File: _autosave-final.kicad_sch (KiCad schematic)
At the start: 25 parts, among them J1 Conn_02x16_Odd_Even, J3 USB_C_Receptacle_USB2.0_14P, SW1 SW_Push, U2 INA219AxD, U3 BQ25601, U4 CH224K

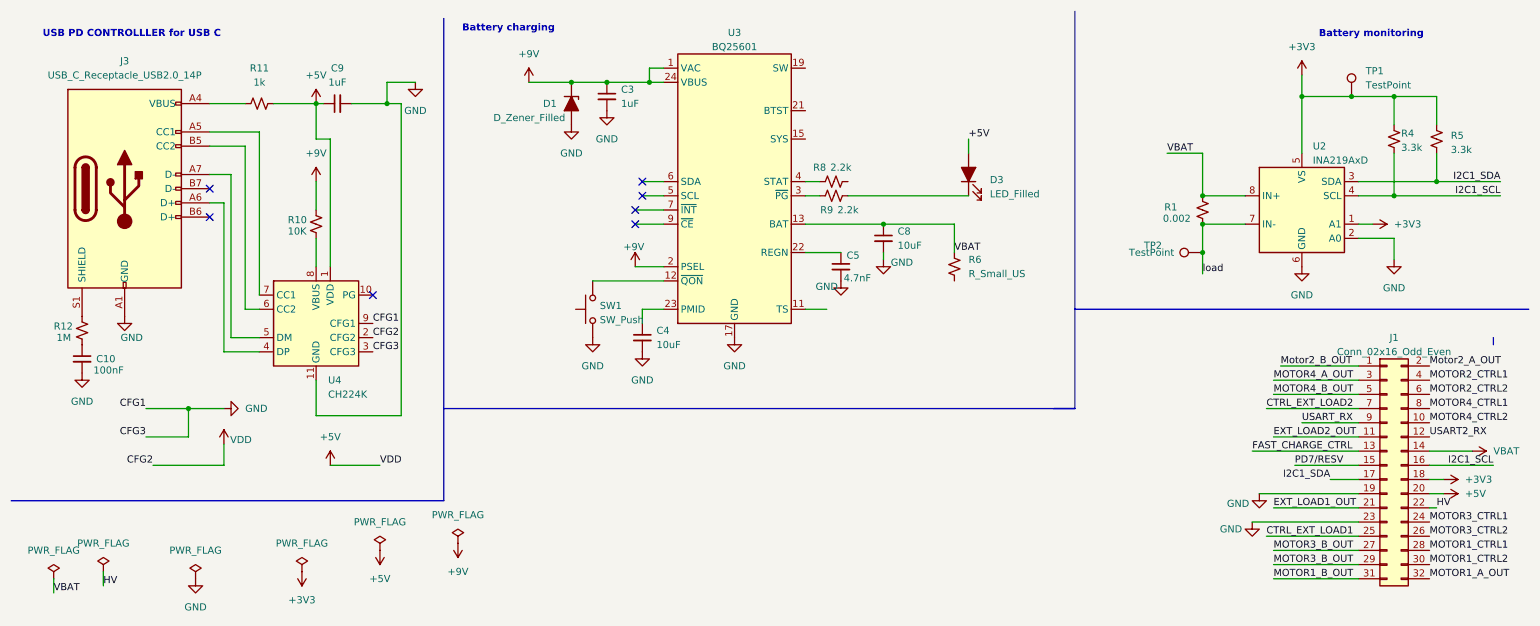
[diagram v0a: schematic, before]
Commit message: i changed my battery monitoring ic
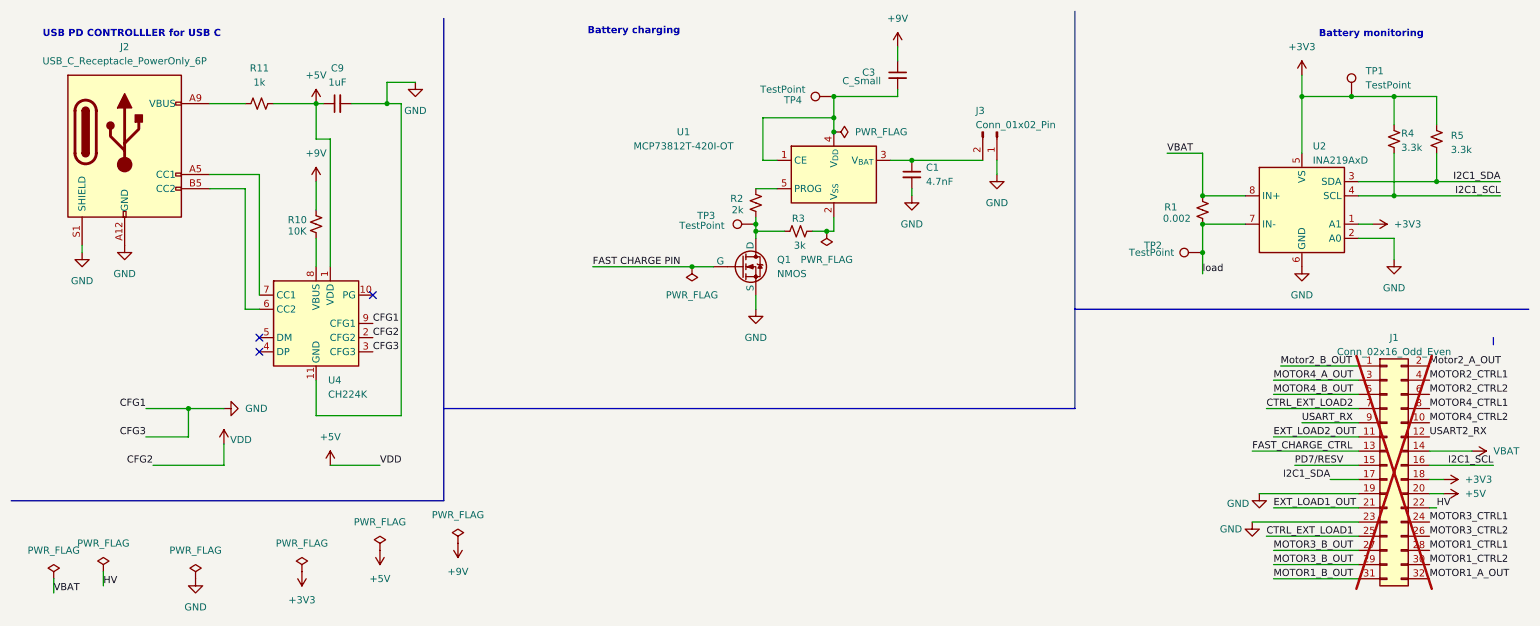
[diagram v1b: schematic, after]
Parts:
- removed C10: 100nF, symbol Device:C_Small
- removed C4: 10uF, Capacitor_SMD:CP_Elec_3x5.3, symbol Device:C_Small
- removed C5: 4.7nF, symbol Device:C_Small
- removed C8: 10uF, symbol Device:C_Small
- removed D1: D_Zener_Filled, symbol Device:D_Zener_Filled
- removed D3: LED_Filled, symbol Device:LED_Filled
- removed J3: USB_C_Receptacle_USB2.0_14P, symbol Connector:USB_C_Receptacle_USB2.0_14P
- removed R12: 1M, symbol Device:R_Small_US
- removed R6: R_Small_US, symbol Device:R_Small_US
- removed R8, R9: 2.2k, symbol Device:R_Small_US
- removed SW1: SW_Push, symbol Switch:SW_Push
- removed U3: BQ25601, Package_DFN_QFN:Texas_S-PWQFN-N24_EP2.7x2.7mm_ThermalVias, symbol Battery_Management:BQ25601
- added C1: 4.7nF, symbol Device:C_Small
- added J2: USB_C_Receptacle_PowerOnly_6P, symbol Connector:USB_C_Receptacle_PowerOnly_6P
- added J3: Conn_01x02_Pin, symbol Connector:Conn_01x02_Pin
- added Q1: NMOS, symbol Simulation_SPICE:NMOS
- added R2: 2k, symbol Device:R_Small_US
- added R3: 3k, symbol Device:R_Small_US
- added TP3, TP4: TestPoint, symbol Connector:TestPoint
- added U1: MCP73812T-420I-OT, Package_TO_SOT_SMD:SOT-23-5, symbol Battery_Management:MCP73812T-420I-OT
- C3: value 1uF -> C_Small; footprint Capacitor_SMD:CP_Elec_3x5.3 -> (none)
- J1: now not fitted
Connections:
- net GND: now also C1.2, J2.A12 (GND), J2.B12 (GND), J2.S1 (SHIELD), J3.1 (Pin_1), Q1.3 (S); no longer C3.2
- net at R11.1: now also J2.A9 (VBUS), J2.B9 (VBUS)
- net at U4.7 (CC1): now also J2.A5 (CC1)
- net at U4.6 (CC2): now also J2.B5 (CC2)
- new net: C1.1, J3.2 (Pin_2), U1.3 (V_{BAT})
- new net: Q1.1 (D), R2.2, R3.1, TP3.1
- new net: R2.1, U1.5 (PROG)
- new net: R3.2, U1.2 (V_{SS})
- new net: C3.2, TP4.1, U1.1 (CE), U1.4 (V_{DD})
- new net FAST CHARGE PIN: Q1.2 (G)
- no-connect marks 7 -> 3
